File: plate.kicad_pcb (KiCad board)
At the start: 2 copper layers, 100 x 59 mm, 57 parts, among them J2 Conn_01x07, J3 Conn_01x06, SW1 SW_Push, SW10 SW_Push, SW11 SW_Push, SW2 SW_Push, SW3 SW_Push, SW4 SW_Push, SW5 SW_Push, SW6 SW_Push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

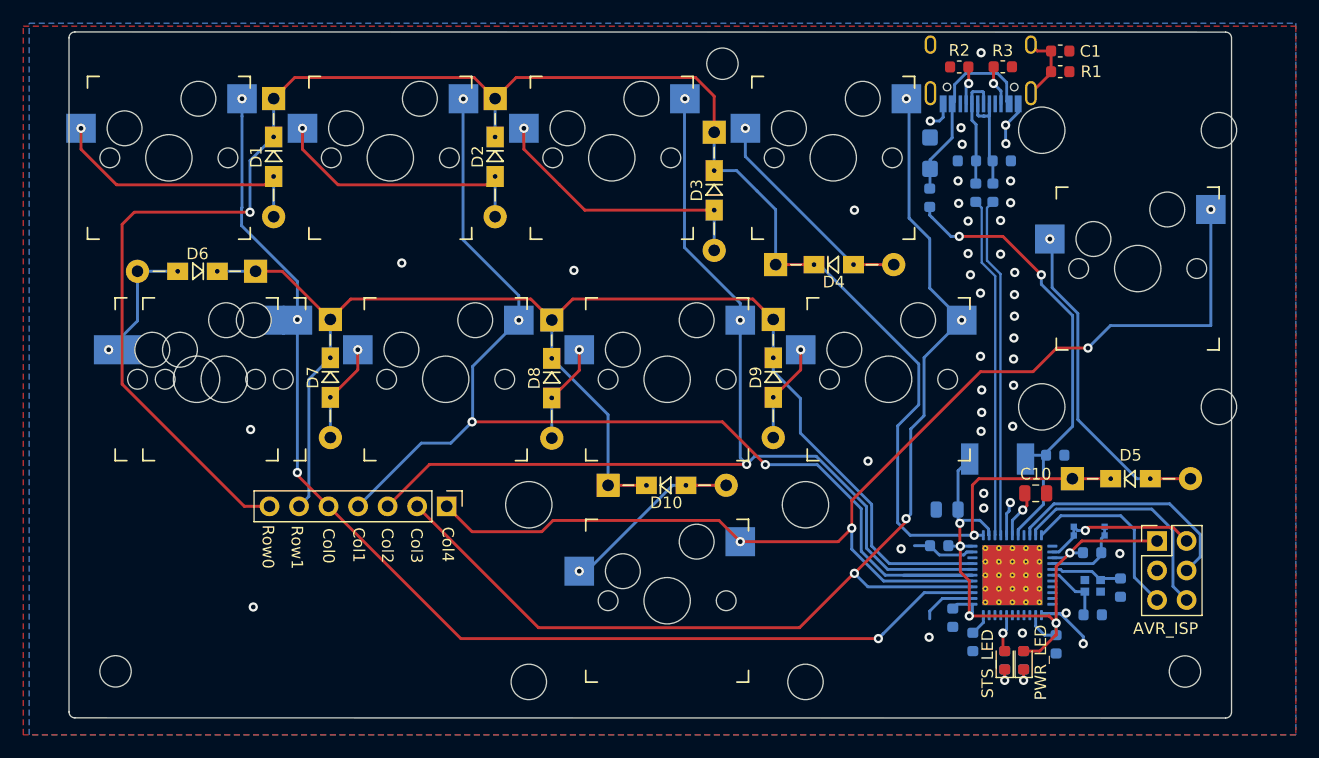
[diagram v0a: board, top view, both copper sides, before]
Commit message: Corrected silkscreen and markings
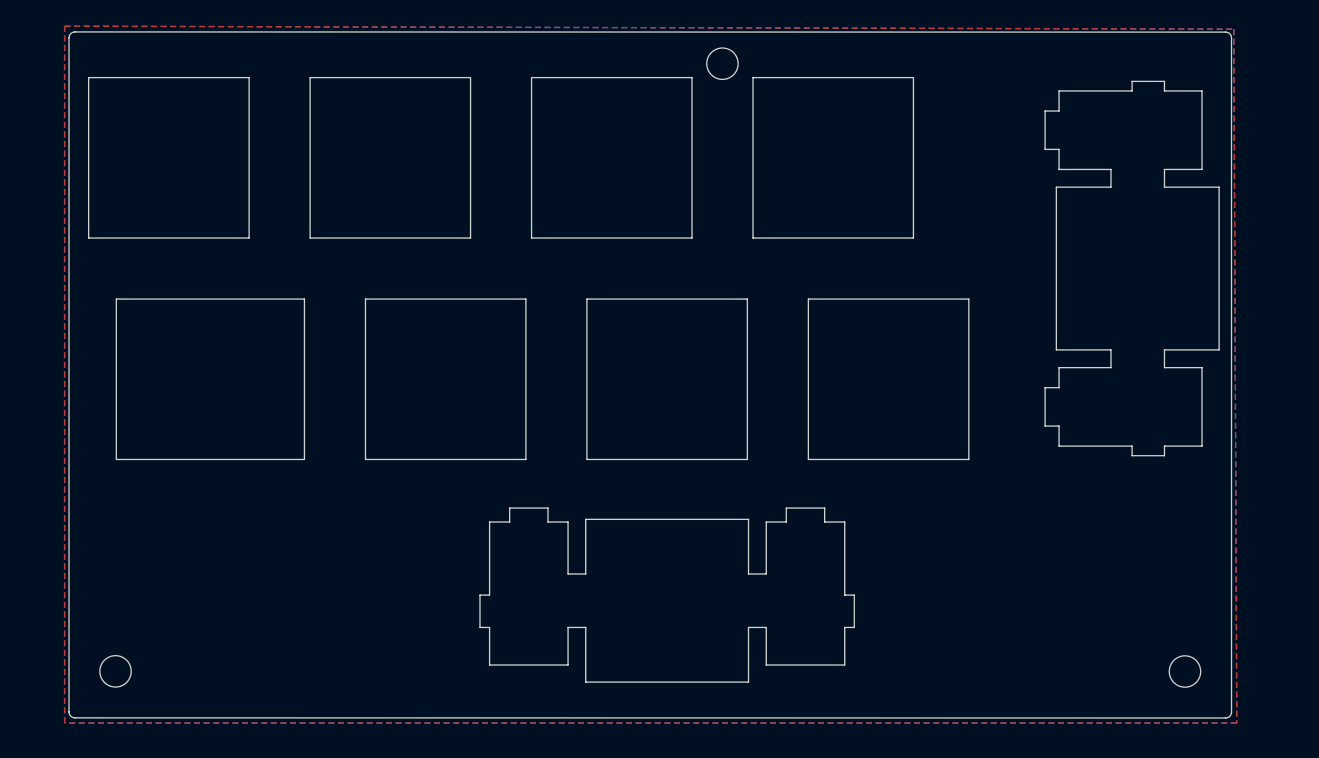
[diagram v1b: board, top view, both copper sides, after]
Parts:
- removed C1, C12, C2, C4, C7, C8: 0u1, Capacitor_SMD:C_0603_1608Metric
- removed C10: 1u, Capacitor_SMD:C_0805_2012Metric
- removed C11: 4u7, Capacitor_SMD:C_0805_2012Metric
- removed C3: 10uF, Capacitor_Tantalum_SMD:CP_EIA-3216-18_Kemet-A
- removed C5, C6: 22p, Capacitor_SMD:C_0603_1608Metric
- removed D1, D10, D2, D3, D4, D5, D6, D7, D8, D9: 1N4148W, Keyboard Library:Diode_DO35_SOD123
- removed F1: 500mA, Fuse:Fuse_0603_1608Metric
- removed J2: Conn_01x07, Connector_PinHeader_2.54mm:PinHeader_1x07_P2.54mm_Vertical
- removed J3: Conn_01x06, Connector_PinHeader_2.54mm:PinHeader_2x03_P2.54mm_Vertical
- removed LED_1: PWR_LED, LED_SMD:LED_0603_1608Metric
- removed LED_2: STS_LED, LED_SMD:LED_0603_1608Metric
- removed R1: 330, Resistor_SMD:R_0603_1608Metric
- removed R11: 10k, Resistor_SMD:R_0603_1608Metric
- removed R13, R7: 33, Resistor_SMD:R_0603_1608Metric
- removed R2, R3: 5k1, Resistor_SMD:R_0603_1608Metric
- removed R4, R5: 22, Resistor_SMD:R_0603_1608Metric
- removed S2: EVP-BB2A9B000, SamacSys_Parts:EVPBB2A9B000
- removed SW10, SW11, SW5: SW_Push, keyswitches:Kailh_socket_MX
- removed U2: ATmega32U4, Package_DFN_QFN:QFN-44-1EP_7x7mm_P0.5mm_EP5.15x5.15mm_ThermalVias
- removed USB1: USB_C_Receptacle_USB2.0, Keyboard Library:HRO-TYPE-C-31-M-12-Assembly
- removed VR1, VR2: CG0603MLC-05E, Resistor_SMD:R_0603_1608Metric
- removed X1: XRCGB16M000FXN00R0, Keyboard Library:XRCGB16M000FXN1R0
- removed ZD1: SM5817-W, Diode_SMD:D_MELF
- ST1, ST2: footprint Keyboard Library:Stabilizer_MX_2u -> Keyboard Library:Cherry_MX_Stabilizer_PCB_2u_placeholder
- SW1, SW2, SW3, SW4, SW7, SW8, SW9: footprint keyswitches:Kailh_socket_MX -> Keyboard Library:Cherry_MX_Plate_Hole_Placeholder
- SW6: footprint keyswitches:Kailh_socket_MX -> Keyboard Library:Cherry_MX_Plate_Hole_Placeholder_1.25
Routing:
- net Row0: track 169.3 -> 0.00 mm, vias 2 -> 0
- net Row1: track 121.7 -> 0.00 mm
- net Col3: track 101.1 -> 0.00 mm, vias 4 -> 0
- net Col1: track 100.8 -> 0.00 mm, vias 4 -> 0
- net Col4: track 100.2 -> 0.00 mm, vias 4 -> 0
- net Col0: track 99.9 -> 0.00 mm, vias 4 -> 0
- net Col2: track 91.9 -> 0.00 mm, vias 3 -> 0
- net VCC: track 56.3 -> 0.00 mm, vias 5 -> 0
- net VBUS: track 39.8 -> 0.00 mm, vias 2 -> 0
- net GND: track 34.2 -> 0.00 mm, vias 42 -> 0
- net /Sheet60039BC7/DD+: track 29.4 -> 0.00 mm
- net /Sheet60039BC7/DD-: track 29.4 -> 0.00 mm
- net Net-(D5-Pad2): track 28.3 -> 0.00 mm, vias 1 -> 0
- net Net-(D3-Pad2): track 23.8 -> 0.00 mm, vias 1 -> 0
- net Net-(D2-Pad2): track 23.4 -> 0.00 mm, vias 1 -> 0
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- added copper zone on B.Cu, net (none)
- added copper zone on F.Cu, net (none)
- removed copper zone on B.Cu, net GND
- removed copper zone on F.Cu, net GND
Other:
- board text removed: "Col0"
- board text removed: "Col1"
- board text removed: "Col2"
- board text removed: "Col3"
- board text removed: "Col4"
- board text removed: "Row0"
- board text removed: "Row1"

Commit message: Update plate.kicad_pcb
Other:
- board text added: "Markus Knutsson 2021 https://github.com/TweetyDaBird Licensed under CERN-OHL-S v2+"
